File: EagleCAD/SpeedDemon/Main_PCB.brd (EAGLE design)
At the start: 77 x 46.5 mm, 77 parts, among them Q1 DMC2700, Q2 BSS138L, U2 NC7S08M, U3 LM3676, U4 STM32F072-LQFP48, X1 32.768kHz

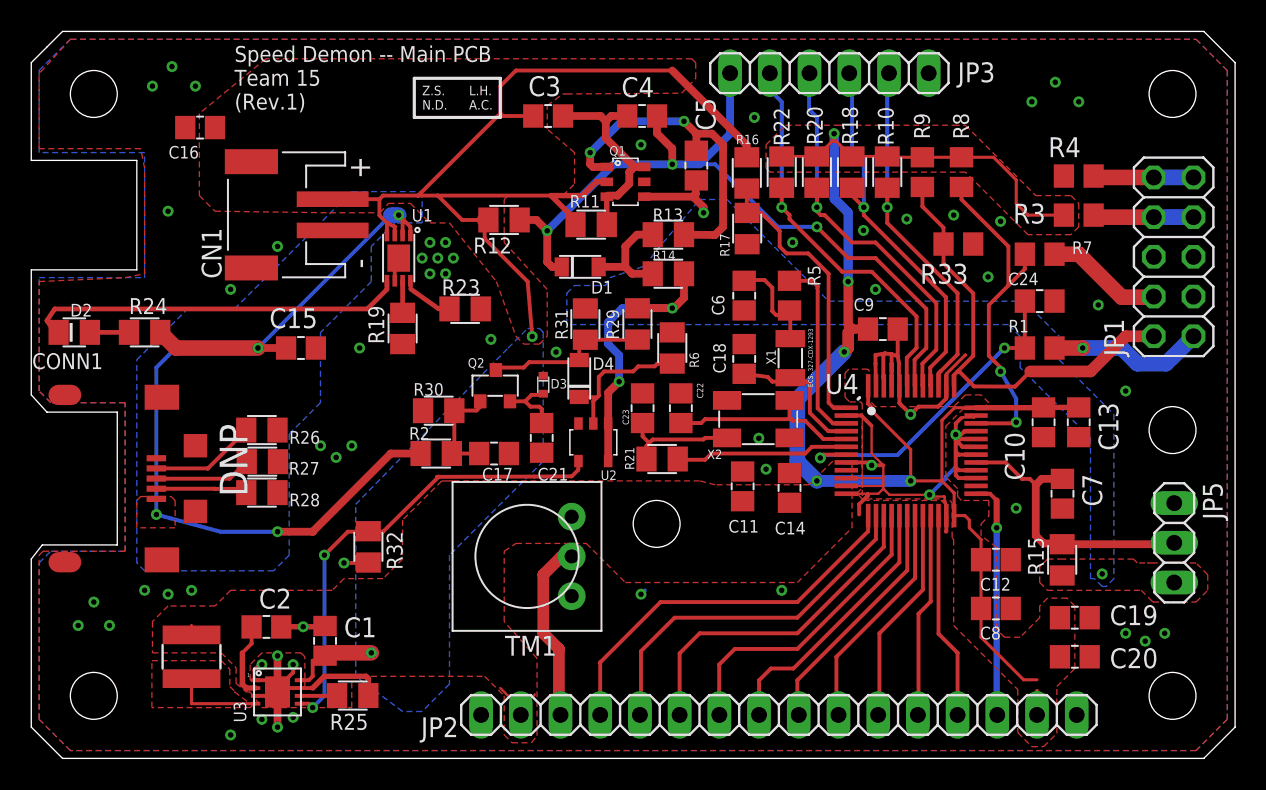
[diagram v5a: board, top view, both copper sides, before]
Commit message: Final Board/schem. Includes added debounce circuit for 5-way switch.
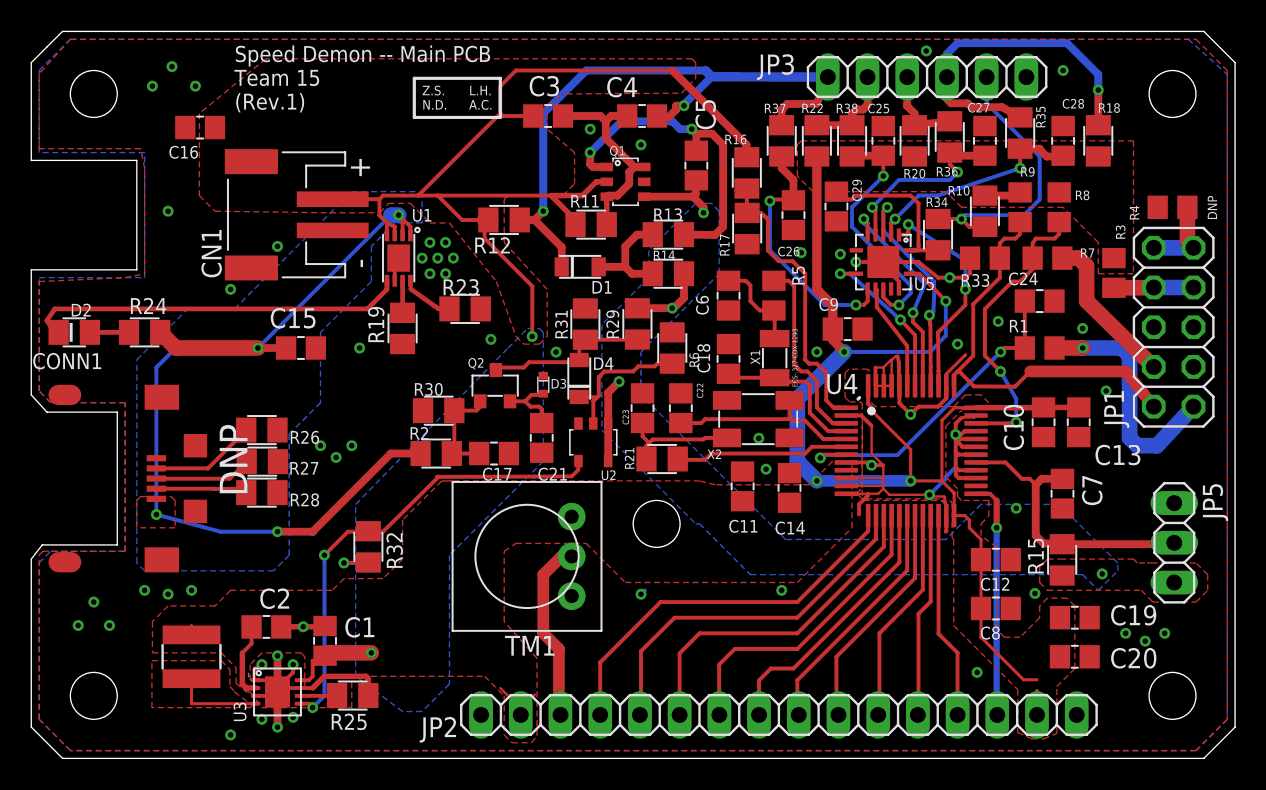
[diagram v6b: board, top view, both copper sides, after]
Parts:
- added C25, C26, C27, C28, C29: 100nF, 0805_generics:C_0805
- added R34, R35, R36, R37, R38: 100, 0805_generics:R_0805
- added U5: (no value), DMC2700:S-PVFQN-N14
- D3: value (none) -> CFSH05
- moved R18 15.9 mm to (68.2, 39.5), turned to 90 degrees
- moved R10 6.73 mm to (61.0, 35.0)
- moved R8 6.64 mm to (65.8, 35.2)
- moved R9 6.64 mm to (63.2, 35.2)
- moved R20 6.56 mm to (56.5, 39.5), turned to 90 degrees
- moved R4 6.32 mm to (73.0, 35.2)
- moved JP3 6.25 mm to (57.3, 43.6)
- moved JP1 4.50 mm to (73.1, 27.6)
- moved R3 4.33 mm to (69.2, 31.1), turned to 90 degrees
- moved R22 3.01 mm to (50.2, 39.5), turned to 90 degrees
- moved C9 2.25 mm to (52.2, 27.5)
- moved R33 1.92 mm to (61.0, 32.0), turned to 0 degrees
- moved C18 1.00 mm to (44.6, 25.6)
- moved C6 1.00 mm to (44.6, 29.6)
- moved R5 1.00 mm to (47.5, 29.6)
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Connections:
- new net N$21: C25.1, R38.1, U5.P$11
- new net N$22: C26.1, R37.1, U5.P$9
- new net N$23: C27.1, R36.2, U5.P$5
- new net N$24: C28.1, R35.2, U5.P$3
- new net N$26: C29.1, R34.2, U5.P$1
- new net PWR_SW_DB: U4.42, U5.P$8
- new net SW_DOWN_DB: U4.40, U5.P$4
- new net SW_LEFT_DB: U4.43, U5.P$10
- new net SW_RIGHT_DB: U4.41, U5.P$6
- new net SW_UP_DB: U4.39, U5.P$2
- net +3V3: now also U5.P$14
- net GND: now also C25.2, C26.2, C27.2, C28.2, C29.2, U5.GND, U5.P$13, U5.P$7
- net PWR_SW: now also R37.2; no longer U4.42
- net SW_DOWN: now also R35.1; no longer U4.40
- net SW_LEFT: now also R38.2; no longer U4.43
- net SW_RIGHT: now also R36.1; no longer U4.41
- net SW_UP: now also R34.1; no longer U4.39
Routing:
- net SW_RIGHT: track 28.0 -> 5.56 mm, vias 1 -> 0
- net SW_LEFT: track 26.5 -> 6.00 mm, vias 1 -> 0
- net N$22: track 0.00 -> 16.4 mm, vias 0 -> 2
- net N$21: track 0.00 -> 16.0 mm, vias 0 -> 2
- net SW_DOWN_DB: track 0.00 -> 14.9 mm, vias 0 -> 2
- net SW_UP_DB: track 0.00 -> 14.5 mm, vias 0 -> 2
- net N$24: track 0.00 -> 14.3 mm, vias 0 -> 2
- net SW_RIGHT_DB: track 0.00 -> 13.8 mm, vias 0 -> 2
- net N$23: track 0.00 -> 12.1 mm, vias 0 -> 2
- net N$26: track 0.00 -> 11.0 mm
- net PWR_SW_DB: track 0.00 -> 10.6 mm, vias 0 -> 2
- net +3V3: track 103.5 -> 93.8 mm, vias 5 -> 4
- net PWR_SW: track 50.3 -> 41.3 mm, vias 3 -> 2
- net VBATT+_SW: track 24.3 -> 15.8 mm
- net GND: track 85.5 -> 93.9 mm, vias 60 -> 61
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
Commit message: tiny revision to final. SUBMITTED THIS VERSION TO FAB.
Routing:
- net N$21: track 16.0 -> 15.4 mm
- net N$24: track 14.3 -> 14.8 mm
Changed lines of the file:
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@@
 <wire x1="55" y1="29" x2="55.5" y2="29" width="0.25" layer="1"/>
 <via x="55.5" y="29" extent="1-16" drill="0.35"/>
-<wire x1="55.5" y1="29" x2="56.25" y2="29.75" width="0.25" layer="16"/>
-<wire x1="56.25" y1="29.75" x2="56.25" y2="30.25" width="0.25" layer="16"/>
-<wire x1="56.25" y1="30.25" x2="52.5" y2="34" width="0.25" layer="16"/>
+<wire x1="55.5" y1="29" x2="55.5" y2="31" width="0.25" layer="16"/>
+<wire x1="55.5" y1="31" x2="52.5" y2="34" width="0.25" layer="16"/>
 <wire x1="52.5" y1="34" x2="52.5" y2="35.25" width="0.25" layer="16"/>
 <wire x1="52.5" y1="35.25" x2="54.5" y2="37.25" width="0.25" layer="16"/>
@@
 <wire x1="63.25" y1="39" x2="63.25" y2="37.75" width="0.25" layer="1"/>
 <via x="63.25" y="37.75" extent="1-16" drill="0.35"/>
-<wire x1="63.25" y1="37.75" x2="58" y2="36" width="0.25" layer="16"/>
-<wire x1="58" y1="36" x2="56.75" y2="36" width="0.25" layer="16"/>
+<wire x1="63.25" y1="37.75" x2="61.75" y2="36" width="0.25" layer="16"/>
+<wire x1="61.75" y1="36" x2="56.75" y2="36" width="0.25" layer="16"/>
 <wire x1="55" y1="33.475" x2="55" y2="34.25" width="0.25" layer="1"/>
 <wire x1="55" y1="34.25" x2="55.25" y2="34.5" width="0.25" layer="1"/>
@@
 <wire x1="56.1" y1="33.65" x2="56.1" y2="34.15" width="0.25" layer="1"/>
 <via x="56.1" y="34.15" extent="1-16" drill="0.35"/>
-<wire x1="56.1" y1="34.15" x2="59.75" y2="31.85" width="0.25" layer="16"/>
+<wire x1="56.1" y1="34.15" x2="57.6" y2="34.15" width="0.25" layer="16"/>
+<wire x1="57.6" y1="34.15" x2="58" y2="33.75" width="0.25" layer="16"/>
+<wire x1="58" y1="33.75" x2="59.75" y2="31.85" width="0.25" layer="16"/>
 <wire x1="59.75" y1="31.85" x2="59.75" y2="30" width="0.25" layer="16"/>
 </signal>
@@
 <via x="54.75" y="35.25" extent="1-16" drill="0.35"/>
 <wire x1="54.75" y1="35.25" x2="54.5" y2="35" width="0.25" layer="16"/>
-<wire x1="54.5" y1="33.75" x2="57.75" y2="30.5" width="0.25" layer="16"/>
-<wire x1="57.75" y1="30.5" x2="57.75" y2="29.5" width="0.25" layer="16"/>
-<wire x1="57.75" y1="29.5" x2="57.7" y2="28.55" width="0.25" layer="16"/>
-<wire x1="57.7" y1="28.55" x2="57.45" y2="28.35" width="0.25" layer="16"/>
+<wire x1="54.5" y1="33.75" x2="57.45" y2="30.75" width="0.25" layer="16"/>
+<wire x1="57.45" y1="30.75" x2="57.45" y2="28.35" width="0.25" layer="16"/>
 <wire x1="54.5" y1="35" x2="54.5" y2="33.75" width="0.25" layer="16"/>
 </signal>
@@
 <wire x1="56.4" y1="27.9" x2="56.4" y2="28.5" width="0.25" layer="1"/>
 <via x="56.4" y="28.5" extent="1-16" drill="0.35"/>
-<wire x1="56.4" y1="28.5" x2="57.15" y2="30.35" width="0.25" layer="16"/>
+<wire x1="56.4" y1="28.5" x2="56.4" y2="31.1" width="0.25" layer="16"/>
 <wire x1="53.25" y1="34.25" x2="53.25" y2="34.5" width="0.25" layer="16"/>
-<wire x1="57.15" y1="30.35" x2="53.25" y2="34.25" width="0.25" layer="16"/>
+<wire x1="56.4" y1="31.1" x2="53.25" y2="34.25" width="0.25" layer="16"/>
 <via x="53.25" y="34.5" extent="1-16" drill="0.35"/>
 <wire x1="53.25" y1="34.5" x2="53.5" y2="34.25" width="0.25" layer="1"/>
@@
 <wire x1="55.6" y1="28.05" x2="56.53" y2="27.07" width="0.25" layer="1"/>
 <wire x1="56.53" y1="27.07" x2="56.53" y2="23.83" width="0.25" layer="1"/>
-<wire x1="55.6" y1="28.05" x2="52.35" y2="31" width="0.25" layer="16"/>
-<wire x1="52.35" y1="31" x2="51.75" y2="31" width="0.25" layer="16"/>
+<wire x1="55.6" y1="28.05" x2="52.1" y2="31" width="0.25" layer="16"/>
+<wire x1="52.1" y1="31" x2="51.75" y2="31" width="0.25" layer="16"/>
 <via x="51.75" y="31" extent="1-16" drill="0.35"/>
 <wire x1="51.75" y1="31" x2="52.775" y2="31" width="0.25" layer="1"/>
